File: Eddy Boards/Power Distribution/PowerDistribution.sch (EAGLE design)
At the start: 1 part

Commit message: Power Distribution Schematic Updates
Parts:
- added 3V3, 5V_LED: (no value), led:LEDCHIPLED_0603
- added 5VCONVERTER: CONVERTER, converter:CONVERTER
- added C16, C17, C18, C7: 47 uF, resistor:C-USC1206K
- added C4: 330 uF, rcl:CPOL-USE5-10.5
- added IC3: REG1117, burr-brown:REG1117
- added L1: 1 uH, inductor-neosid:MS85
- added Q10: MOSFET-NCH-AO3404A, SparkFun-DiscreteSemi:MOSFET-NCH-AO3404A
- added R22: 100K, rcl:R-US_R0603
- added R23: 13K, rcl:R-US_R0603
- added R24: 90, rcl:R-US_R0603
- added R28: (no value), rcl:R-TRIMM3103
- added R32: 5, rcl:R-US_R0603
- added U$2: XT90PWH, XT90:XT90PWH
- added U$4: 14PIN-VERT, Vertical_Connectors:14PIN-VERT
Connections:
- new net 5VON: Q10.G, R22.2, R23.2, U$1.5V_ON_OFF
- new net BALANCED_OUT: L1.1, R22.1
- new net MOTOR_POWER: U$4.1+, U$4.2+, U$4.3+, U$4.4+, U$4.5+, U$4.6+, U$4.7+
- new net N$14: 5VCONVERTER.6,TRIM, R28.A
- new net N$19: 5VCONVERTER.2,ON/OFF, Q10.D
- new net N$24: 5VCONVERTER.1,VIN(+), C4.+, L1.2
- new net N$25: 5V_LED.A, R24.1
- new net N$28: 3V3.A, R32.1
- net +3V3: now also C7.1, IC3.VOUT, R32.2
- net +5V: now also 5VCONVERTER.7,SENSE+, 5VCONVERTER.8,VOUT(+), C16.1, C17.1, C18.1, IC3.VIN, R24.2
- net GND: now also 3V3.C, 5VCONVERTER.3,VIN(-)/GND, 5VCONVERTER.4,VOUT(-)/GND, 5V_LED.C, C16.2, C17.2, C18.2, C4.-, C7.2, IC3.GND, Q10.S, R23.1, R28.S, U$4.1-, U$4.2-, U$4.3-, U$4.4-, U$4.5-, U$4.6-, U$4.7-

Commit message: Power Distribution DC Converter Work
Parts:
- removed 5VCONVERTER: CONVERTER, converter:CONVERTER
- removed 5V_LED: (no value), led:LEDCHIPLED_0603
- removed C16, C17, C18: 47 uF, resistor:C-USC1206K
- removed L1: 1 uH, inductor-neosid:MS85
- removed Q10: MOSFET-NCH-AO3404A, SparkFun-DiscreteSemi:MOSFET-NCH-AO3404A
- removed R22: 100K, rcl:R-US_R0603
- removed R23: 13K, rcl:R-US_R0603
- removed R24: 90, rcl:R-US_R0603
- removed R28: (no value), rcl:R-TRIMM3103
- added 12V_LED: (no value), led:LEDCHIPLED_0603
- added C1: (no value), adafruit:CPOL-USE5-10.5
- added C2: 47uF, adafruit:CPOL-USE5-10.5
- added C3: 1.5nF, rcl:C-EUC0603
- added C5: 470uF, rcl:C-EUC0603
- added C6: 0.01uF, rcl:C-EUC0603
- added C8: (no value), rcl:C-EUC0603
- added Q1: 5.8A/30V/35mΩ, SparkFun-DiscreteSemi:MOSFET-NCH-AO3404A
- added R1, R3: 100K, audio amplifier example:R-US_R0603
- added R2: 6.19K, resistor:R-TRIMM3103
- added R4: 13K, audio amplifier example:R-US_R0603
- added R5: 470, audio amplifier example:R-US_R0603
- added R6: 200, audio amplifier example:R-US_R0603
- added U$3: DC_DC_CONVERTER, DC_DC_CONVERTER:DC_DC_CONVERTER
- C4: value 330 uF -> 22uF; device rcl:CPOL-USE5-10.5 -> rcl:C-EUC0603
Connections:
- removed net N$14: 5VCONVERTER.6,TRIM, R28.A
- removed net N$19: 5VCONVERTER.2,ON/OFF, Q10.D
- removed net N$24: 5VCONVERTER.1,VIN(+), C4.+, L1.2
- removed net N$25: 5V_LED.A, R24.1
- new net 12VON: 12V_LED.C, C1.-, C2.-, C4.1, C5.1, C6.1, C8.1, Q1.S, R2.E, R3.2, R4.1, U$1.12V_ON/OFF, U$3.GRND
- new net N$3: 12V_LED.A, R5.1
- new net N$4: C3.1, R6.1
- new net N$5: Q1.D, R1.1, U$3.ON/OFF
- new net N$6: C3.2, R2.A, U$3.TRIM
- new net N$7: Q1.G, R4.2
- new net N$8: C1.+, C4.2, C5.2, R5.2, R6.2, U$3.VOUT, U$3.VS+
- new net V+: C2.+, C6.2, C8.2, R1.2, U$3.VIN
- net +5V: no longer 5VCONVERTER.7,SENSE+, 5VCONVERTER.8,VOUT(+), C16.1, C17.1, C18.1, R24.2
- net 5VON: no longer Q10.G, R22.2, R23.2
- net BALANCED_OUT: now also R3.1; no longer L1.1, R22.1
- net GND: now also U$3.SYNC; no longer 5VCONVERTER.3,VIN(-)/GND, 5VCONVERTER.4,VOUT(-)/GND, 5V_LED.C, C16.2, C17.2, C18.2, C4.-, Q10.S, R23.1, R28.S

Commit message: Eddy PD Work
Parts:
- removed C7: 47 uF, resistor:C-USC1206K
- removed R32: 5, rcl:R-US_R0603
- added 5V_LED1: (no value), led:LEDCHIPLED_0603
- added C10: 47uF, adafruit:CPOL-USE5-10.5
- added C11: 12nF, rcl:C-EUC0603
- added C12: 22uF, rcl:C-EUC0603
- added C13, C15: 330uF, rcl:C-EUC0603
- added C14: 0.01uF, rcl:C-EUC0603
- added C16: 47 uF, resistor:C-USC1206K
- added KILLSWITCH_LED: (no value), led:LEDCHIP-LED0603
- added Q2: 5.8A/30V/35mΩ, SparkFun-DiscreteSemi:MOSFET-NCH-AO3404A
- added Q3, Q5: SPB80P06P, transistor-fet:SPB80P06P
- added Q4: 310mA/60V/1.6Ω, SparkFun-DiscreteSemi:MOSFET-NCH-2N7002PW
- added R10: 90, audio amplifier example:R-US_R0603
- added R11: 200, audio amplifier example:R-US_R0603
- added R12: 13K, audio amplifier example:R-US_R0603
- added R13: 5, rcl:R-US_R0603
- added R14, R15: 10K, rcl:R-US_R0603
- added R16: 68, rcl:R-US_R0603
- added R7, R9: 100K, audio amplifier example:R-US_R0603
- added R8: 16.27, resistor:R-TRIMM3103
- added U$5: DC_DC_CONVERTER, DC_DC_CONVERTER:DC_DC_CONVERTER
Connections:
- removed net BALANCED_OUT: R3.1
- new net +12V: C1.+, C10.+, C14.2, C15.2, C4.2, C5.2, R5.2, R6.2, R7.2, U$3.VOUT, U$3.VS+, U$5.VIN
- new net KILL_SWITCH: Q4.S, R16.2
- new net N$1: Q4.D, R14.1
- new net N$10: 5V_LED1.A, R10.1
- new net N$11: C11.1, R11.1
- new net N$16: KILLSWITCH_LED.C, R16.1
- new net N$9: C11.2, R8.A, U$5.TRIM
- net +3V3: now also C16.1, KILLSWITCH_LED.A, Q4.G, R13.2; no longer C7.1, R32.2
- net +5V: now also C12.2, C13.2, R10.2, R11.2, U$5.VOUT, U$5.VS+
- net 12VON: now also Q1.G, R4.2; no longer 12V_LED.C, C1.-, C2.-, C4.1, C5.1, C6.1, C8.1, Q1.S, R2.E, R4.1, U$3.GRND
- net 5VON: now also Q2.G, R12.2, R9.2
- net GND: now also 12V_LED.C, 5V_LED1.C, C1.-, C10.-, C12.1, C13.1, C14.1, C15.1, C16.2, C2.-, C4.1, C5.1, C6.1, C8.1, Q1.S, Q2.S, R12.1, R2.E, R4.1, R8.E, U$2.GND, U$3.GRND, U$5.GRND, U$5.SYNC; no longer C7.2
- net MOTOR_POWER: now also Q3.D, Q5.D
- net N$28: now also R13.1; no longer R32.1
- net N$7: now also Q2.D, R7.1, U$5.ON/OFF; no longer Q1.G, R4.2
- net N$8: now also Q3.G, Q5.G, R14.2, R15.1; no longer C1.+, C4.2, C5.2, R5.2, R6.2, U$3.VOUT, U$3.VS+
- net V+: now also Q3.S, Q5.S, R15.2, R3.1, R9.1, U$2.V+

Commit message: Power Distribution Changes
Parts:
- removed 5V_LED1: (no value), led:LEDCHIPLED_0603
- removed C10: 47uF, adafruit:CPOL-USE5-10.5
- removed C11: 12nF, rcl:C-EUC0603
- removed C12: 22uF, rcl:C-EUC0603
- removed C13, C15: 330uF, rcl:C-EUC0603
- removed C14: 0.01uF, rcl:C-EUC0603
- removed R10: 90, audio amplifier example:R-US_R0603
- removed R11, R6: 200, audio amplifier example:R-US_R0603
- removed R12: 13K, audio amplifier example:R-US_R0603
- removed R7, R9: 100K, audio amplifier example:R-US_R0603
- removed R8: 16.27, resistor:R-TRIMM3103
- removed U$5: DC_DC_CONVERTER, DC_DC_CONVERTER:DC_DC_CONVERTER
- added 5V_LED: (no value), led:LEDCHIPLED_0603
- added C17, C9: 1 uF, rcl:C-EUC0603
- added C18, C19, C20, C21: 22uF, rcl:C-EUC0603
- added C7: 22 uF, rcl:C-EUC0603
- added L1: 5.0 uH, inductor-neosid:MS85
- added L2: 2.8uH, inductor-neosid:MS85
- added Q6, Q7: 5.8A/30V/35mΩ, SparkFun-DiscreteSemi:MOSFET-NCH-AO3404A
- added R17: 10K, audio amplifier example:R-US_R0603
- added R18: 160K, audio amplifier example:R-US_R0603
- added R19: 100K, audio amplifier example:R-US_R0603
- added R20: 25K, audio amplifier example:R-US_R0603
- added R21: 470, audio amplifier example:R-US_R0603
- added U$6: RT7258-2, RT7258-2:RT7258-2
- C1: value (none) -> 22 uF; device adafruit:CPOL-USE5-10.5 -> rcl:C-EUC0603
- C2: value 47uF -> 1 uF; device adafruit:CPOL-USE5-10.5 -> rcl:C-EUC0603
- C3: value 1.5nF -> 1 uF
- C5: value 470uF -> 22uF
- C6: value 0.01uF -> 22uF
- C8: value (none) -> 22uF
- R1: value 100K -> 18K
- R13: value 5 -> 5.6
- R2: value 6.19K -> 93K; device resistor:R-TRIMM3103 -> audio amplifier example:R-US_R0603
- R4: value 13K -> 25K
- R5: value 470 -> 100
- U$3: value DC_DC_CONVERTER -> RT7258-2; device DC_DC_CONVERTER:DC_DC_CONVERTER -> RT7258-2:RT7258-2
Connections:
- new net BG: Q1.G, U$3.BG
- new net BG2: Q6.G, U$6.BG
- new net N$12: C9.2, U$6.VCC
- new net N$13: 12V_LED.A, R21.1
- new net N$14: C17.2, U$6.BOOT
- new net N$15: Q7.D, U$6.EN/SYNC
- new net N$17: C19.1, C20.2
- new net N$18: C20.1, C21.2
- new net N$19: C18.1, C19.2
- new net N$20: R17.2, R18.1, U$6.FB
- new net V+1: C17.1, L1.1, Q6.D, U$6.SW
- new net V+2: C3.1, L2.1, Q1.D, U$3.SW
- net +12V: now also C1.2, C18.2, L1.2, R18.2, R21.2, U$3.VIN; no longer C1.+, C10.+, C14.2, C15.2, C4.2, C5.2, R5.2, R6.2, R7.2, U$3.VOUT, U$3.VS+, U$5.VIN
- net +5V: now also C4.2, L2.2, R2.2, R5.2; no longer C12.2, C13.2, R10.2, R11.2, U$5.VOUT, U$5.VS+
- net 12VON: now also Q7.G, R19.2, R20.2; no longer Q1.G, R3.2, R4.2
- net 5VON: now also R3.2, R4.2; no longer R12.2, R9.2
- net GND: now also 5V_LED.C, C1.1, C2.1, C21.1, C7.1, C9.1, Q6.S, Q7.S, R1.1, R17.1, R20.1, U$3.GND, U$3.PGOOD, U$6.GND, U$6.PGOOD; no longer 5V_LED1.C, C1.-, C10.-, C12.1, C13.1, C14.1, C15.1, C2.-, C4.1, C5.1, C6.1, R12.1, R2.E, R8.E, U$3.GRND, U$3.SYNC, U$5.GRND, U$5.SYNC
- net N$10: now also R1.2, R2.1, U$3.FB; no longer 5V_LED1.A, R10.1
- net N$11: now also 5V_LED.A, R5.1; no longer C11.1, R11.1
- net N$3: now also C2.2, U$3.VCC; no longer 12V_LED.A, R5.1
- net N$4: now also C3.2, U$3.BOOT; no longer C3.1, R6.1
- net N$5: now also Q2.D, U$3.EN/SYNC; no longer Q1.D, R1.1, U$3.ON/OFF
- net N$6: now also C5.1, C6.2; no longer C3.2, R2.A, U$3.TRIM
- net N$7: now also C6.1, C8.2; no longer Q2.D, R7.1, U$5.ON/OFF
- net N$9: now also C4.1, C5.2; no longer C11.2, R8.A, U$5.TRIM
- net V+: now also C7.2, R19.1, U$6.VIN; no longer C2.+, C6.2, C8.2, R1.2, R9.1, U$3.VIN
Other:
- moved on the sheet: 12V_LED, 3V3, C16, C3, C4, C5, C6, C8, IC3, Q1, Q2, R1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

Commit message: Power Distribution
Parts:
- removed Q2: 5.8A/30V/35mΩ, SparkFun-DiscreteSemi:MOSFET-NCH-AO3404A
- removed R3: 100K, audio amplifier example:R-US_R0603
- removed R4: 25K, audio amplifier example:R-US_R0603
- added Q8: 5.8A/30V/35mΩ, SparkFun-DiscreteSemi:MOSFET-NCH-AO3404A
- added R6: 100K, audio amplifier example:R-US_R0603
- added R7: 25K, audio amplifier example:R-US_R0603
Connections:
- removed net N$15: Q7.D, U$6.EN/SYNC
- removed net N$5: Q2.D, U$3.EN/SYNC
- new net 12EN: Q7.S, R19.2, R20.2, U$6.EN/SYNC
- new net 5VEN: Q8.S, R6.2, R7.2, U$3.EN/SYNC
- net 12VON: no longer R19.2, R20.2
- net 5VON: now also Q8.G; no longer Q2.G, R3.2, R4.2
- net GND: now also Q7.D, Q8.D, R7.1; no longer Q2.S, Q7.S, R4.1
- net V+: now also R6.1; no longer R3.1
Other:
- moved on the sheet: Q7, R19, R20

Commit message: Eddy BB Update
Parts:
- added X1: 5566-4, con-molex:5566-4
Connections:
- net +12V: now also X1-4.S
- net +5V: now also X1-3.S
- net GND: now also X1-1.S, X1-2.S
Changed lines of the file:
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@@
 <part name="GND21" library="supply1" library_urn="urn:adsk.eagle:library:371" deviceset="GND" device=""/>
 <part name="GND22" library="supply1" library_urn="urn:adsk.eagle:library:371" deviceset="GND" device=""/>
+<part name="GND18" library="supply1" library_urn="urn:adsk.eagle:library:371" deviceset="GND" device=""/>
+<part name="P+2" library="supply1" library_urn="urn:adsk.eagle:library:371" deviceset="+5V" device=""/>
+<part name="P+12" library="supply1" library_urn="urn:adsk.eagle:library:371" deviceset="+12V" device=""/>
+<part name="X1" library="con-molex" library_urn="urn:adsk.eagle:library:165" deviceset="5566-4" device="" package3d_urn="urn:adsk.eagle:package:8078582/1"/>
 </parts>
 <sheets>
@@
 <attribute name="VALUE" x="287.02" y="144.78" size="1.778" layer="96" rot="R180"/>
 </instance>
+<instance part="GND18" gate="1" x="63.5" y="200.66" smashed="yes" rot="R270">
+<attribute name="VALUE" x="60.96" y="203.2" size="1.778" layer="96" rot="R270"/>
+</instance>
+<instance part="P+2" gate="1" x="63.5" y="193.04" smashed="yes" rot="R90">
+<attribute name="VALUE" x="63.5" y="195.58" size="1.778" layer="96" rot="R180"/>
+</instance>
+<instance part="P+12" gate="1" x="63.5" y="187.96" smashed="yes" rot="R90">
+<attribute name="VALUE" x="63.5" y="190.5" size="1.778" layer="96" rot="R180"/>
+</instance>
+<instance part="X1" gate="-1" x="73.66" y="203.2" smashed="yes">
+<attribute name="NAME" x="76.2" y="202.438" size="1.524" layer="95"/>
+<attribute name="VALUE" x="72.898" y="204.597" size="1.778" layer="96"/>
+</instance>
+<instance part="X1" gate="-2" x="73.66" y="198.12" smashed="yes">
+<attribute name="NAME" x="76.2" y="197.358" size="1.524" layer="95"/>
+</instance>
+<instance part="X1" gate="-3" x="73.66" y="193.04" smashed="yes">
+<attribute name="NAME" x="76.2" y="192.278" size="1.524" layer="95"/>
+</instance>
+<instance part="X1" gate="-4" x="73.66" y="187.96" smashed="yes">
+<attribute name="NAME" x="76.2" y="187.198" size="1.524" layer="95"/>
+</instance>
 </instances>
 <busses>
@@
 <pinref part="P+1" gate="1" pin="+5V"/>
 <wire x1="30.48" y1="64.77" x2="30.48" y2="71.12" width="0.1524" layer="91"/>
+</segment>
+<segment>
+<pinref part="P+2" gate="1" pin="+5V"/>
+<pinref part="X1" gate="-3" pin="S"/>
+<wire x1="71.12" y1="193.04" x2="66.04" y2="193.04" width="0.1524" layer="91"/>
 </segment>
 </net>
@@
 <pinref part="U$2" gate="G$1" pin="GND"/>
 <wire x1="289.56" y1="137.16" x2="297.18" y2="137.16" width="0.1524" layer="91"/>
+</segment>
+<segment>
+<pinref part="GND18" gate="1" pin="GND"/>
+<wire x1="66.04" y1="200.66" x2="68.58" y2="200.66" width="0.1524" layer="91"/>
+<wire x1="68.58" y1="200.66" x2="68.58" y2="203.2" width="0.1524" layer="91"/>
+<pinref part="X1" gate="-1" pin="S"/>
+<wire x1="68.58" y1="203.2" x2="71.12" y2="203.2" width="0.1524" layer="91"/>
+<wire x1="68.58" y1="200.66" x2="68.58" y2="198.12" width="0.1524" layer="91"/>
+<junction x="68.58" y="200.66"/>
+<pinref part="X1" gate="-2" pin="S"/>
+<wire x1="68.58" y1="198.12" x2="71.12" y2="198.12" width="0.1524" layer="91"/>
 </segment>
 </net>
@@
 </segment>
 </net>
+<net name="+12V" class="0">
+<segment>
+<pinref part="P+12" gate="1" pin="+12V"/>
+<pinref part="X1" gate="-4" pin="S"/>
+<wire x1="71.12" y1="187.96" x2="66.04" y2="187.96" width="0.1524" layer="91"/>
+</segment>
+</net>

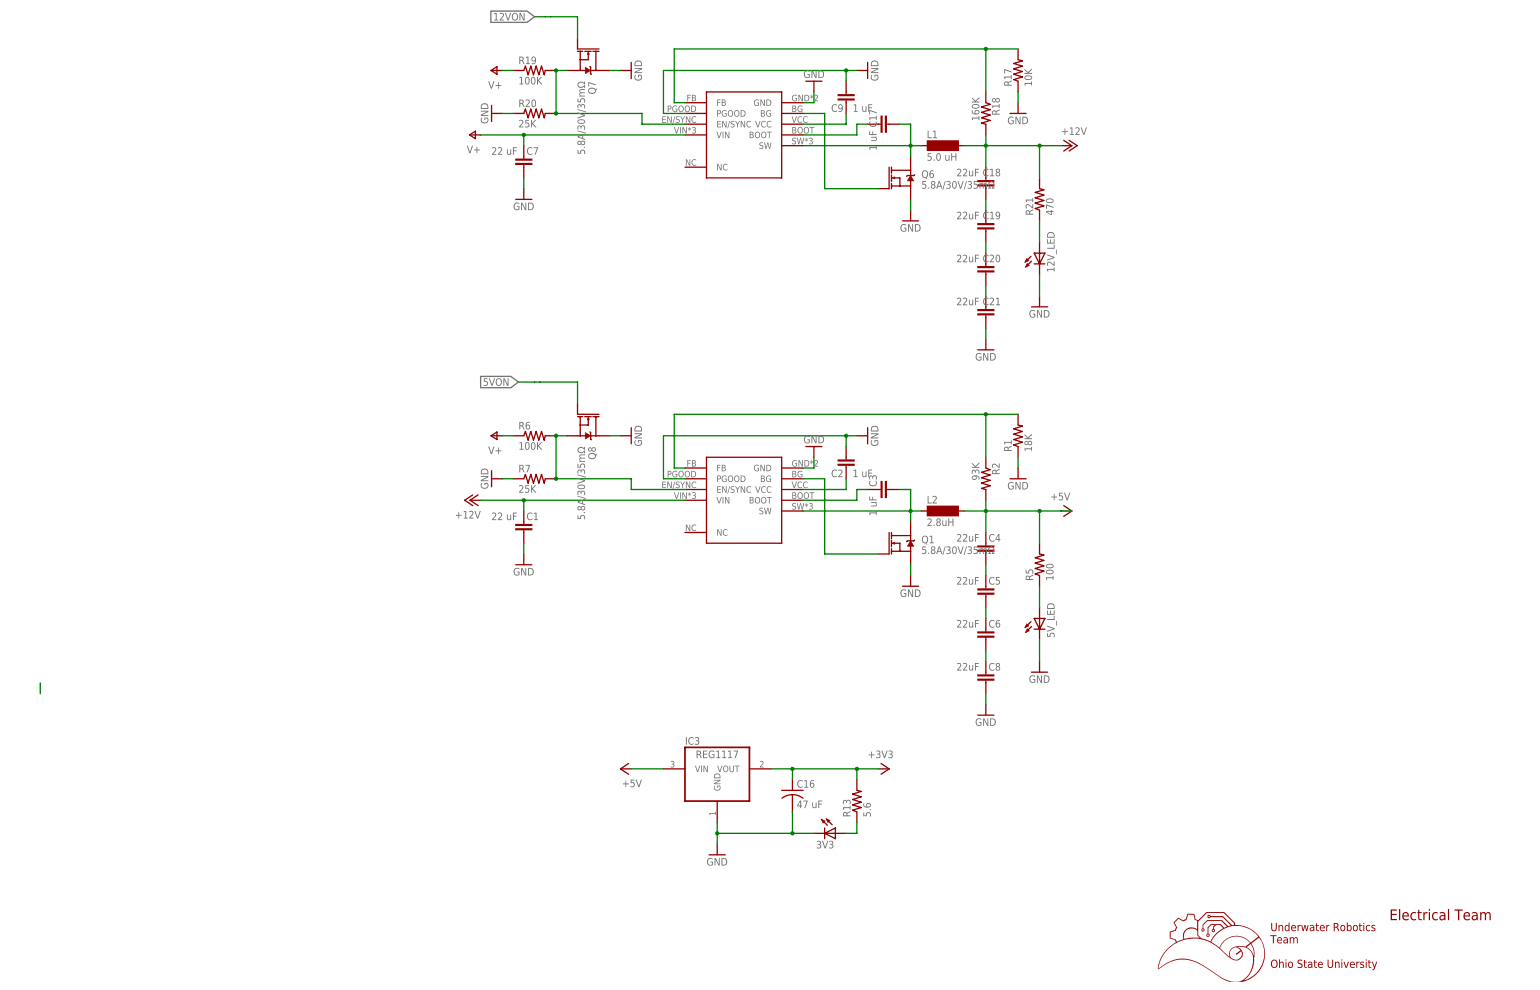
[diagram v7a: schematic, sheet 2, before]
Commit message: Eddy Power Distribution Review Changes
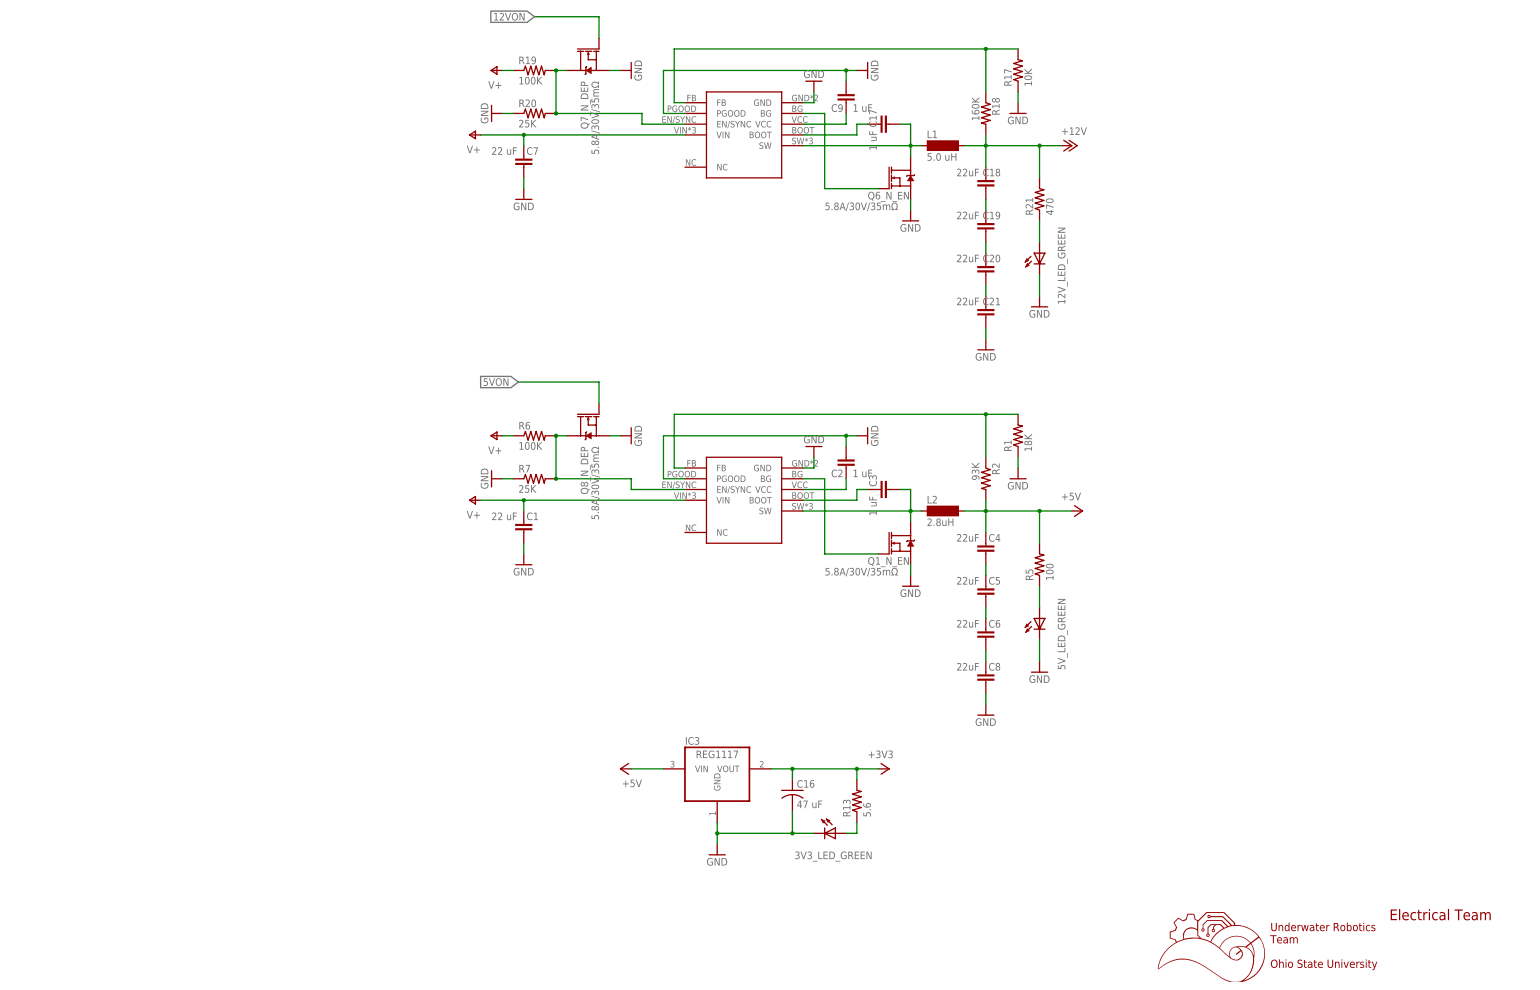
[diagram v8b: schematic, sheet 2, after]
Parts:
- renumbered 12V_LED to 12V_LED_GREEN, 3V3 to 3V3_LED_GREEN, 5V_LED to 5V_LED_GREEN, Q1 to Q1_N_EN, Q6 to Q6_N_EN, Q7 to Q7_N_DEP, Q8 to Q8_N_DEP
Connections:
- net +12V: no longer C1.2, U$3.VIN
- net 12EN: now also Q7_N_DEP.D; no longer Q7_N_DEP.S
- net 5VEN: now also Q8_N_DEP.D; no longer Q8_N_DEP.S
- net GND: now also Q7_N_DEP.S, Q8_N_DEP.S; no longer Q7_N_DEP.D, Q8_N_DEP.D
- net KILL_SWITCH: now also U$1.KILL_SWITCH
- net V+: now also C1.2, U$3.VIN
